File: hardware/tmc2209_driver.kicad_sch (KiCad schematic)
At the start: 33 parts

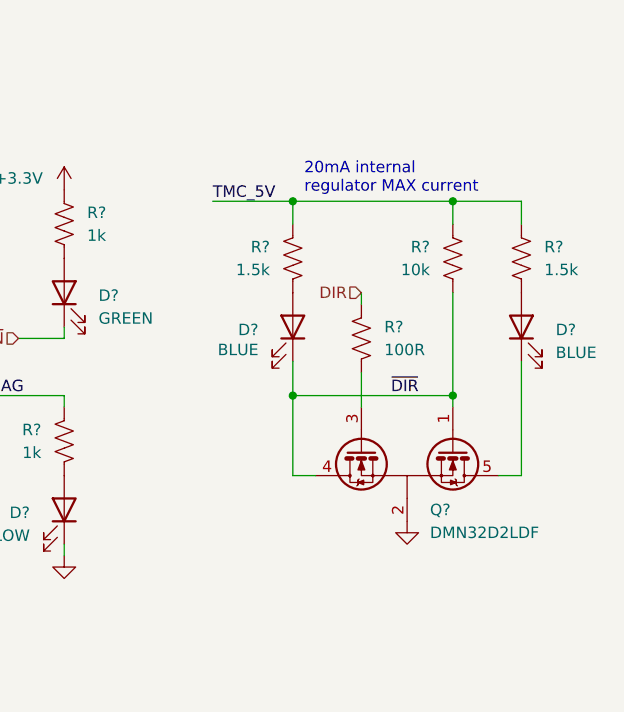
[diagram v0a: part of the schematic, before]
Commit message: Change blue LEDs
Remove extra 5V blue LED driving for simple 3.3V driving instead
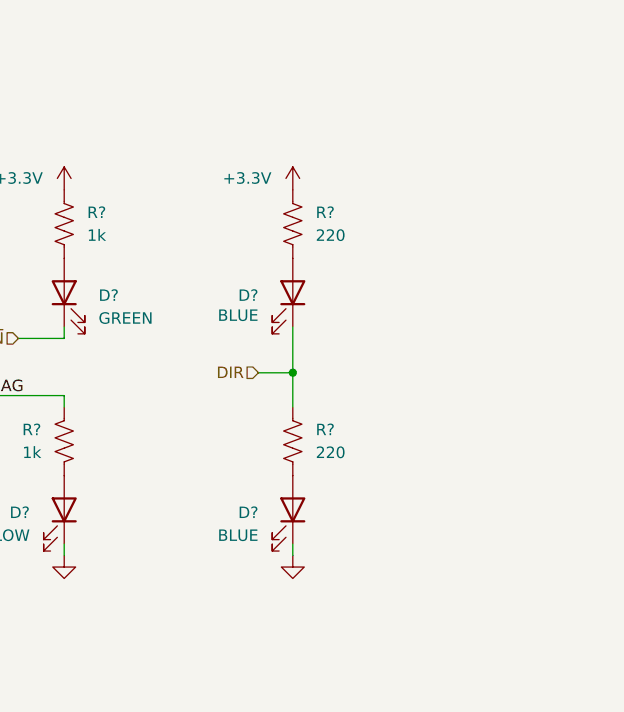
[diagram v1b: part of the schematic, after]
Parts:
- removed Q?: DMN32D2LDF, Package_TO_SOT_SMD:SOT-353_SC-70-5, symbol Transistor_FET:DMN32D2LDF
- removed R? (x2): 1.5k, Resistor_SMD:R_0603_1608Metric, symbol Device:R_US
- removed R?: 10k, Resistor_SMD:R_0603_1608Metric, symbol Device:R_US
- removed R?: 100R, Resistor_SMD:R_0603_1608Metric, symbol Device:R_US
- added R? (x2): 220, Resistor_SMD:R_0603_1608Metric, symbol Device:R_US
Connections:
- net ~{DIR} is gone; now on net DIR: D?.1 (K)
- net +3.3V: now also R?.1
- net DIR: now also R?.1
- net GND: now also D?.1 (K)
- net at D?.2 (A): now also R?.2 (x2)
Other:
- note removed: "20mA internal regulator MAX current"
- moved on the sheet: D?

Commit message: Add QSPI Flash
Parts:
- gave numbers to parts that had none: 30

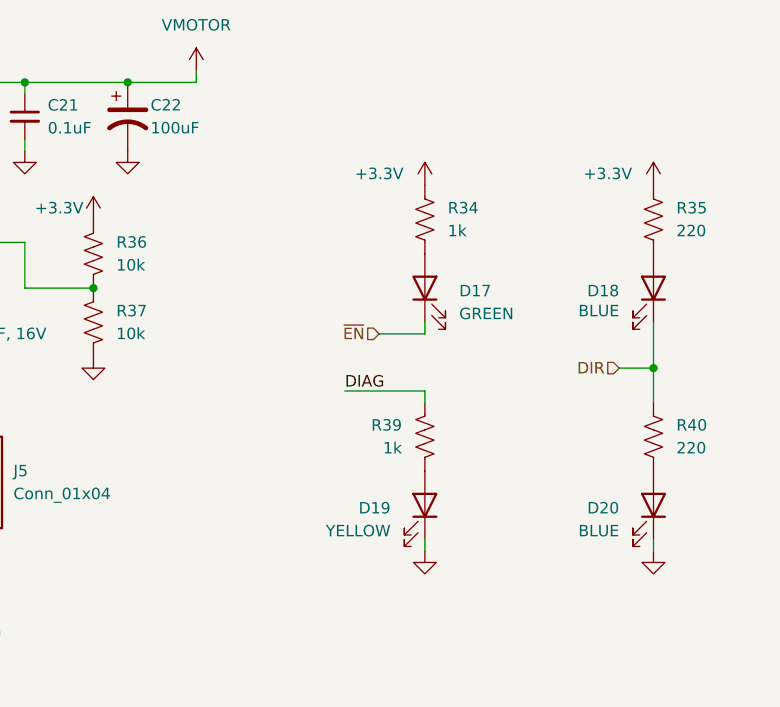
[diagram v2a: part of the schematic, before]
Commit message: Adjust power input protection
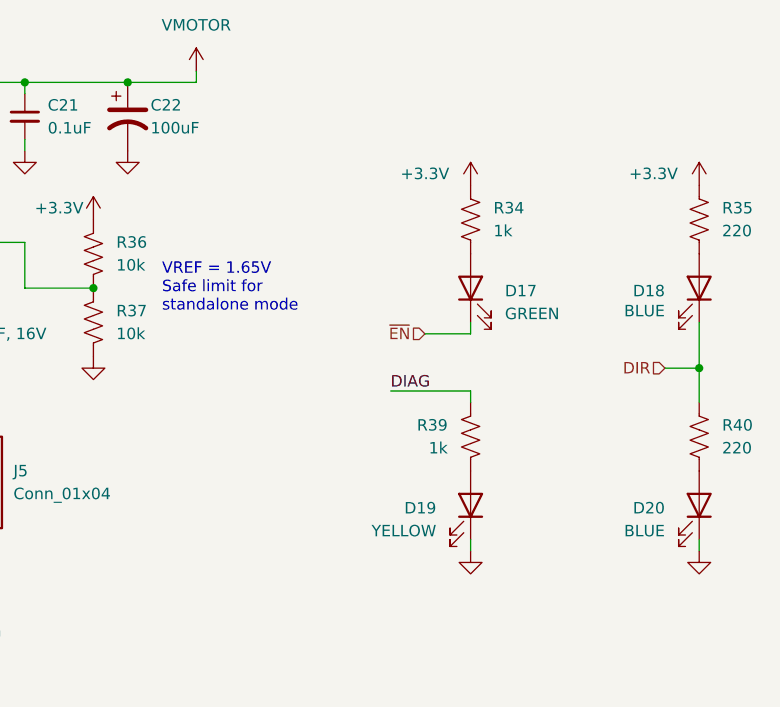
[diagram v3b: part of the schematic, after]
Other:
- note added: "VREF = 1.65V Safe limit for standalone mode"
- moved on the sheet: D17, D18, D19, D20, R34, R35, R39, R40
